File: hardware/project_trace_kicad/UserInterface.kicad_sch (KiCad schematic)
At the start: 13 parts, among them J601 Conn_01x14_Socket, J602 Conn_01x14_Pin, SW601 SW_Push, SW602 SW_Push, SW603 RotaryEncoder, SW604 RotaryEncoder, U601 SBC-OLED01.3

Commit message: Partnumbers and BOM updated
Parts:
- J601: DigikeyPN 455-1590-1-ND -> 455-1576-1-ND
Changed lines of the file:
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@@
 			)
 		)
-		(property "DigikeyPN" "455-1590-1-ND"
+		(property "DigikeyPN" "455-1576-1-ND"
 			(at 74.93 118.11 0)
 			(hide yes)

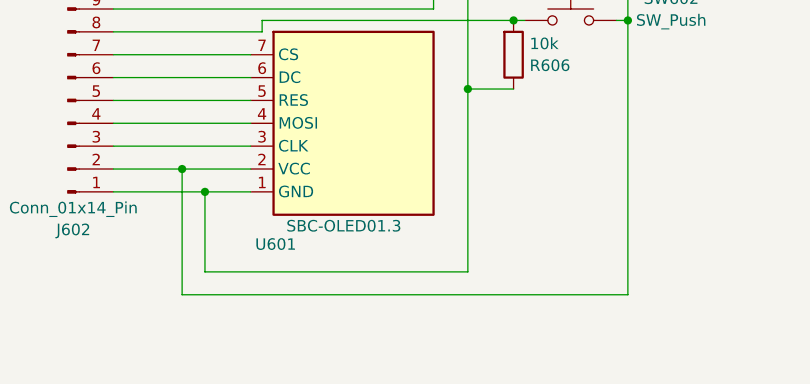
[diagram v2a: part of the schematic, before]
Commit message: Implement new DiffAmp, Small Improvements
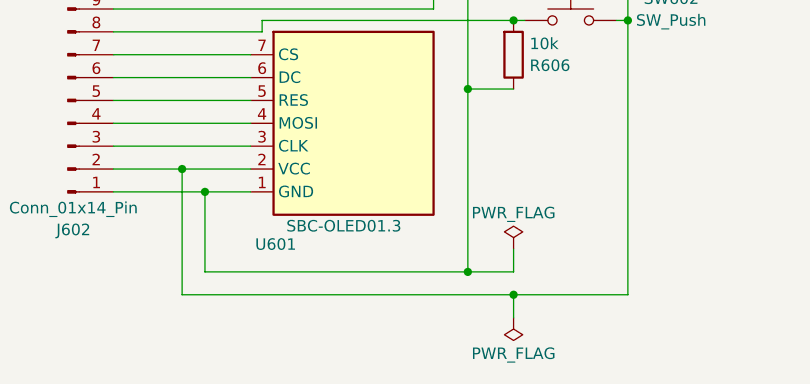
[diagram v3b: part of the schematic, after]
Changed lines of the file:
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@@
+	)
+	(junction
+		(at 147.32 144.78)
+		(diameter 0)
+		(color 0 0 0 0)
 	)
 	(junction
@@
 	)
 	(junction
+		(at 142.24 142.24)
+		(diameter 0)
+		(color 0 0 0 0)
+	)
+	(junction
 		(at 147.32 101.6)
 		(diameter 0)
@@
 	(wire
 		(pts
-			(xy 110.49 144.78) (xy 160.02 144.78)
+			(xy 110.49 144.78) (xy 147.32 144.78)
 		)
 		(stroke
@@
 	(wire
 		(pts
+			(xy 147.32 144.78) (xy 160.02 144.78)
+		)
+		(stroke
+			(width 0)
+			(type default)
+		)
+	)
+	(wire
+		(pts
 			(xy 152.4 44.45) (xy 151.13 44.45)
 		)
@@
 	(wire
 		(pts
+			(xy 147.32 144.78) (xy 147.32 147.32)
+		)
+		(stroke
+			(width 0)
+			(type default)
+		)
+	)
+	(wire
+		(pts
 			(xy 142.24 73.66) (xy 143.51 73.66)
 		)
@@
 	(wire
 		(pts
+			(xy 147.32 142.24) (xy 142.24 142.24)
+		)
+		(stroke
+			(width 0)
+			(type default)
+		)
+	)
+	(wire
+		(pts
 			(xy 154.94 82.55) (xy 157.48 82.55)
 		)
@@
 		(pts
 			(xy 151.13 73.66) (xy 152.4 73.66)
+		)
+		(stroke
+			(width 0)
+			(type default)
+		)
+	)
+	(wire
+		(pts
+			(xy 147.32 139.7) (xy 147.32 142.24)
 		)
 		(stroke
@@
 	)
 	(symbol
+		(lib_id "power:PWR_FLAG")
+		(at 147.32 139.7 0)
+		(unit 1)
+		(body_style 1)
+		(exclude_from_sim no)
+		(in_bom yes)
+		(on_board yes)
+		(in_pos_files yes)
+		(dnp no)
+		(fields_autoplaced yes)
+		(property "Reference" "#FLG0601"
+			(at 147.32 137.795 0)
+			(hide yes)
+			(show_name no)
+			(do_not_autoplace no)
+			(effects
+				(font
+					(size 1.27 1.27)
+				)
+			)
+		)
+		(property "Value" "PWR_FLAG"
+			(at 147.32 135.6952 0)
+			(show_name no)
+			(do_not_autoplace no)
+			(effects
+				(font
+					(size 1.27 1.27)
+				)
+			)
+		)
+		(property "Footprint" ""
+			(at 147.32 139.7 0)
+			(hide yes)
+			(show_name no)
+			(do_not_autoplace no)
+			(effects
+				(font
+					(size 1.27 1.27)
+				)
+			)
+		)
+		(property "Datasheet" ""
+			(at 147.32 139.7 0)
+			(hide yes)
+			(show_name no)
+			(do_not_autoplace no)
+			(effects
+				(font
+					(size 1.27 1.27)
+				)
+			)
+		)
+		(property "Description" "Special symbol for telling ERC where power comes from"
+			(at 147.32 139.7 0)
+			(hide yes)
+			(show_name no)
+			(do_not_autoplace no)
+			(effects
+				(font
+					(size 1.27 1.27)
+				)
+			)
+		)
+		(pin "1"
+		)
+		(instances
+			(project "project_trace_kicad"
+				(path "/af51f4e5-b952-4b0e-baf2-78a72fb86fcd/9647d892-1f14-4449-8bb1-1c7676664973"
+					(reference "#FLG0601")
+					(unit 1)
+				)
+			)
+		)
+	)
+	(symbol
 		(lib_id "Device:R")
 		(at 147.32 106.68 0)
@@
 					(unit 1)
 				)
+			)
+		)
+	)
+	(symbol
+		(lib_id "power:PWR_FLAG")
+		(at 147.32 147.32 0)
+		(mirror x)
+		(unit 1)
+		(body_style 1)
+		(exclude_from_sim no)
+		(in_bom yes)
+		(on_board yes)
+		(in_pos_files yes)
+		(dnp no)
+		(property "Reference" "#FLG0602"
+			(at 147.32 149.225 0)
+			(hide yes)
+			(show_name no)
+			(do_not_autoplace no)
+			(effects
+				(font
+					(size 1.27 1.27)
+				)
+			)
+		)
+		(property "Value" "PWR_FLAG"
+			(at 147.32 151.3248 0)
+			(show_name no)
+			(do_not_autoplace no)
+			(effects
+				(font
+					(size 1.27 1.27)
+				)
+			)
+		)
+		(property "Footprint" ""
+			(at 147.32 147.32 0)
+			(hide yes)
+			(show_name no)
+			(do_not_autoplace no)
+			(effects
+				(font
+					(size 1.27 1.27)
+				)
+			)
+		)
+		(property "Datasheet" ""
+			(at 147.32 147.32 0)
+			(hide yes)
+			(show_name no)
+			(do_not_autoplace no)
+			(effects
+				(font
+					(size 1.27 1.27)
+				)
+			)
+		)
+		(property "Description" "Special symbol for telling ERC where power comes from"
+			(at 147.32 147.32 0)
+			(hide yes)
+			(show_name no)
+			(do_not_autoplace no)
+			(effects
+				(font
+					(size 1.27 1.27)
+				)
+			)
+		)
+		(pin "1"
+		)
+		(instances
+			(project "project_trace_kicad"
+				(path "/af51f4e5-b952-4b0e-baf2-78a72fb86fcd/9647d892-1f14-4449-8bb1-1c7676664973"
+					(reference "#FLG0602")
+					(unit 1)
+				)

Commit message: Changes to Digital
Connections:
- net UI.GND: now reaches J602.1 (Pin_1), R605.2, R606.1, U601.1 (GND)
- net UI.GND: now also SW603.C, SW604.C; no longer R601.1, R602.1, R603.1, R604.2
- net UI.VCC: now reaches J602.2 (Pin_2), SW601.2, SW602.1, U601.2 (VCC)
- net UI.VCC: now also R601.2, R602.2, R603.1, R604.2; no longer SW603.C, SW604.C
- net at J602.12 (Pin_12), SW603.B: now also R601.1; no longer R602.2
- net at J602.13 (Pin_13), SW603.A: now also R602.1; no longer R601.2
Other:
- moved on the sheet: R601, R602, R603, R604, R605, R606, SW601, SW603, SW604

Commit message: Unfinished change of UI connectivity
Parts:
- removed J601: Conn_01x14_Socket, ProjectTraceFootprints:JST_BM14B-GHS-TBT_LF__SN__N_, symbol Connector:Conn_01x14_Socket
- removed J602: Conn_01x14_Pin, symbol Connector:Conn_01x14_Pin
- removed R605, R606: 10k, Resistor_THT:R_Axial_DIN0207_L6.3mm_D2.5mm_P10.16mm_Horizontal, symbol Device:R
- removed SW601: SW_Push, symbol Switch:SW_Push
- added SW603: SW_Push, symbol Switch:SW_Push
- added UIC601, UIC602, UIC603, UIC604, UIC605, UIC606, UIC607, UIC608, UIC609, UIC610, UIC611, UIC612, UIC613, UIC614, UIC615, UIC616, UIC617, UIC618, UIC619, UIC620, UIC621: UIconnector, TestPoint:TestPoint_Pad_D2.5mm, symbol Connector:TestPoint
- renumbered SW603 to SW601
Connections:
- net +3V3: now also R601.1, R602.2, R603.1, R604.1
- net Disp.CLK: now also U601.3 (CLK), UIC610.1
- net Disp.DC: now also U601.6 (DC), UIC604.1
- net Disp.MOSI: now also U601.4 (MOSI), UIC608.1
- net Disp.RES: now also U601.5 (RES), UIC606.1
- net Disp.~{CS}: now also U601.7 (CS), UIC602.1
- net SW1: now also UIC619.1
- net SW2: now also UIC616.1
- net SW3.A: now also R601.2, UIC614.1
- net SW3.B: now also R602.1, UIC615.1
- net SW4.A: now also R603.2, UIC617.1
- net SW4.B: now also R604.2, UIC618.1
- net UI.GND: now also SW602.1, SW603.2, UIC601.1, UIC603.1, UIC605.1, UIC607.1, UIC609.1, UIC611.1, UIC613.1, UIC620.1, UIC621.1
- net UI.VCC: now also UIC612.1; no longer R601.2, R602.2, R603.1, R604.2, SW602.1
- net at SW604.A: no longer R603.2
- net at SW601.A: no longer R602.1
- net at SW604.B: no longer R604.1
- net at SW601.B: no longer R601.1
- no-connect marks 2 -> 6
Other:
- note added: "Off-board"
- note added: "Pullup from MCU"
- note removed: "CLK"
- note removed: "CS"
- note removed: "DC"
- note removed: "GND"
- note removed: "MOSI"
- note removed: "NC"
- note removed: "RES"
- note removed: "VCC"
- moved on the sheet: SW601, SW602, SW604, U601

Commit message: Review 1 issues adressed
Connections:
- net +3V3: now also UIC612.1
- net UI.GND: no longer UIC601.1, UIC603.1, UIC605.1, UIC607.1, UIC609.1, UIC611.1, UIC613.1, UIC620.1, UIC621.1
- net UI.VCC: no longer UIC612.1
- new net GND: UIC601.1, UIC603.1, UIC605.1, UIC607.1, UIC609.1, UIC611.1, UIC613.1, UIC620.1, UIC621.1
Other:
- moved on the sheet: UIC601, UIC602, UIC603, UIC604, UIC605, UIC606, UIC607, UIC608, UIC609, UIC610, UIC611, UIC612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

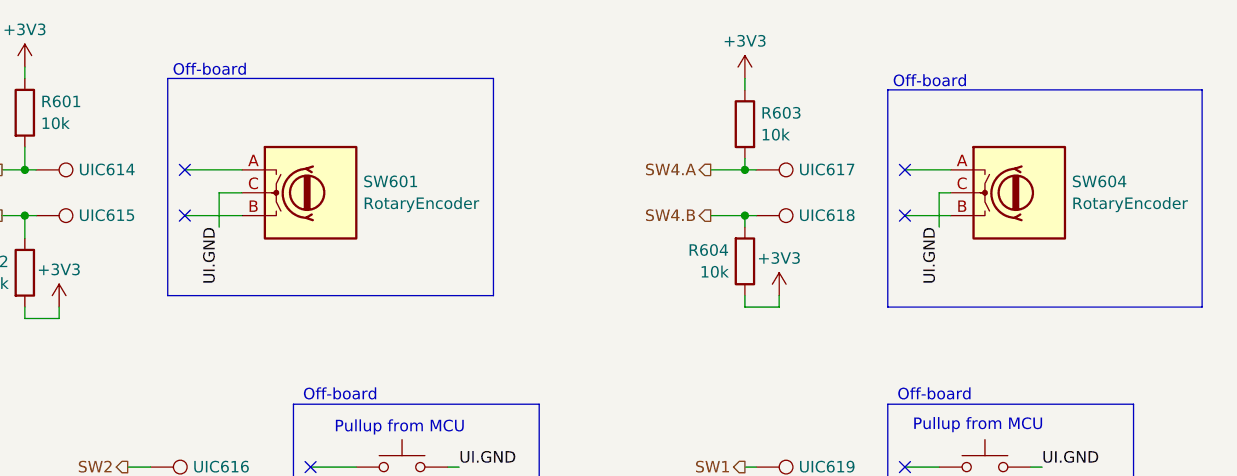
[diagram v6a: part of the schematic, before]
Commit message: Address items of internal review
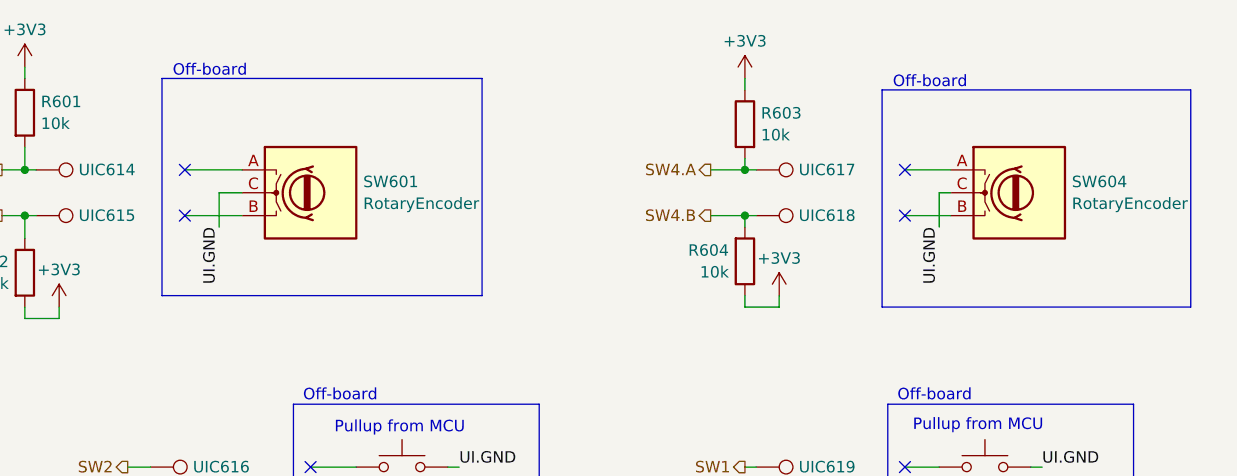
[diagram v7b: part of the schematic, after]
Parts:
- R601, R602, R603, R604: footprint Resistor_THT:R_Axial_DIN0207_L6.3mm_D2.5mm_P10.16mm_Horizontal -> Resistor_SMD:R_0603_1608Metric_Pad0.98x0.95mm_HandSolder; DigikeyPN (none) -> YAG1236CT-ND
- SW601, SW602, SW603, SW604, U601: DigikeyPN (none) -> N/A
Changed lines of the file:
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@@
 	(title_block
 		(title "Multilloscope - UserInterface")
-		(date "2026-04-06")
-		(comment 1 "Alexander N. Olsen")
+		(date "2026-04-19")
+		(rev "2")
+		(comment 1 "Reviewed by Laurits K. Hillemann")
+		(comment 2 "Alexander N. Olsen")
 	)
 	(rectangle
@@
 	)
 	(rectangle
-		(start 146.685 48.26)
-		(end 182.88 72.39)
+		(start 146.05 48.26)
+		(end 181.61 72.39)
 		(stroke
 			(width 0)
@@
 	)
 	(rectangle
-		(start 226.695 49.53)
-		(end 261.62 73.66)
+		(start 226.06 49.53)
+		(end 260.35 73.66)
 		(stroke
 			(width 0)
@@
 			)
 		)
+		(property "DigikeyPN" "N/A"
+			(at 172.72 91.44 0)
+			(hide yes)
+			(show_name no)
+			(do_not_autoplace no)
+			(effects
+				(font
+					(size 1.27 1.27)
+				)
+			)
+		)
 		(pin "2"
 		)
@@
 		(exclude_from_sim no)
 		(in_bom yes)
-		(on_board no)
+		(on_board yes)
 		(in_pos_files yes)
 		(dnp no)
@@
 			)
 		)
-		(property "Footprint" "Resistor_THT:R_Axial_DIN0207_L6.3mm_D2.5mm_P10.16mm_Horizontal"
+		(property "Footprint" "Resistor_SMD:R_0603_1608Metric_Pad0.98x0.95mm_HandSolder"
 			(at 129.032 69.85 90)
 			(hide yes)
@@
 			)
 		)
+		(property "DigikeyPN" "YAG1236CT-ND"
+			(at 130.81 69.85 0)
+			(hide yes)
+			(show_name no)
+			(do_not_autoplace no)
+			(effects
+				(font
+					(size 1.27 1.27)
+				)
+			)
+		)
 		(pin "2"
 		)
@@
 			)
 		)
+		(property "DigikeyPN" "N/A"
+			(at 162.56 60.96 0)
+			(hide yes)
+			(show_name no)
+			(do_not_autoplace no)
+			(effects
+				(font
+					(size 1.27 1.27)
+				)
+			)
+		)
 		(pin "B"
 		)
@@
 			)
 		)
+		(property "DigikeyPN" "N/A"
+			(at 241.3 60.96 0)
+			(hide yes)
+			(show_name no)
+			(do_not_autoplace no)
+			(effects
+				(font
+					(size 1.27 1.27)
+				)
+			)
+		)
 		(pin "B"
 		)
@@
 		(exclude_from_sim no)
 		(in_bom yes)
-		(on_board no)
+		(on_board yes)
 		(in_pos_files yes)
 		(dnp no)
@@
 			)
 		)
-		(property "Footprint" "Resistor_THT:R_Axial_DIN0207_L6.3mm_D2.5mm_P10.16mm_Horizontal"
+		(property "Footprint" "Resistor_SMD:R_0603_1608Metric_Pad0.98x0.95mm_HandSolder"
 			(at 209.042 68.58 90)
 			(hide yes)
@@
 			)
 		)
+		(property "DigikeyPN" "YAG1236CT-ND"
+			(at 210.82 68.58 0)
+			(hide yes)
+			(show_name no)
+			(do_not_autoplace no)
+			(effects
+				(font
+					(size 1.27 1.27)
+				)
+			)
+		)
 		(pin "2"
 		)
@@
 		(exclude_from_sim no)
 		(in_bom yes)
-		(on_board no)
+		(on_board yes)
 		(in_pos_files yes)
 		(dnp no)
@@
 			)
 		)
-		(property "Footprint" "Resistor_THT:R_Axial_DIN0207_L6.3mm_D2.5mm_P10.16mm_Horizontal"
+		(property "Footprint" "Resistor_SMD:R_0603_1608Metric_Pad0.98x0.95mm_HandSolder"
 			(at 129.032 52.07 90)
 			(hide yes)
@@
 			)
 		)
+		(property "DigikeyPN" "YAG1236CT-ND"
+			(at 130.81 52.07 0)
+			(hide yes)
+			(show_name no)
+			(do_not_autoplace no)
+			(effects
+				(font
+					(size 1.27 1.27)
+				)
+			)
+		)
 		(pin "2"
 		)
@@
 		(exclude_from_sim no)
 		(in_bom yes)
-		(on_board no)
+		(on_board yes)
 		(in_pos_files yes)
 		(dnp no)
@@
 			)
 		)
-		(property "Footprint" "Resistor_THT:R_Axial_DIN0207_L6.3mm_D2.5mm_P10.16mm_Horizontal"
+		(property "Footprint" "Resistor_SMD:R_0603_1608Metric_Pad0.98x0.95mm_HandSolder"
 			(at 212.598 53.34 90)
 			(hide yes)
@@
 			)
 		)
+		(property "DigikeyPN" "YAG1236CT-ND"
+			(at 210.82 53.34 0)
+			(hide yes)
+			(show_name no)
+			(do_not_autoplace no)
+			(effects
+				(font
+					(size 1.27 1.27)
+				)
+			)
+		)
 		(pin "2"
 		)
@@
 			)
 		)
+		(property "DigikeyPN" "N/A"
+			(at 116.84 143.51 0)
+			(hide yes)
+			(show_name no)
+			(do_not_autoplace no)
+			(effects
+				(font
+					(size 1.27 1.27)
+				)
+			)
+		)
 		(pin "4"
 		)
@@
 			(at 237.49 91.44 0)
 			(hide yes)
+			(show_name no)
+			(do_not_autoplace no)
+			(effects
+				(font
+					(size 1.27 1.27)
+				)
+			)
+		)
+		(property "DigikeyPN" "N/A"
+			(at 237.49 91.44 0)
+			(hide yes)

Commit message: Small Fixes, Fabrication File Check
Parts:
- renumbered UIC620 to UIC617, UIC621 to UIC618, UIC617 to UIC619, UIC618 to UIC620, UIC619 to UIC621
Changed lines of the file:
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@@
 		(dnp no)
 		(fields_autoplaced yes)
-		(property "Reference" "#PWR0604"
+		(property "Reference" "#PWR0607"
 			(at 214.63 76.2 0)
 			(hide yes)
@@
 			(project "project_trace_kicad"
 				(path "/af51f4e5-b952-4b0e-baf2-78a72fb86fcd/9647d892-1f14-4449-8bb1-1c7676664973"
-					(reference "#PWR0604")
+					(reference "#PWR0607")
 					(unit 1)
 				)
@@
 		(dnp no)
 		(fields_autoplaced yes)
-		(property "Reference" "#PWR0606"
+		(property "Reference" "#PWR0601"
 			(at 99.06 116.84 0)
 			(hide yes)
@@
 			(project "project_trace_kicad"
 				(path "/af51f4e5-b952-4b0e-baf2-78a72fb86fcd/9647d892-1f14-4449-8bb1-1c7676664973"
-					(reference "#PWR0606")
+					(reference "#PWR0601")
 					(unit 1)
 				)
@@
 		(dnp no)
 		(fields_autoplaced yes)
-		(property "Reference" "#PWR0602"
+		(property "Reference" "#PWR0604"
 			(at 134.62 77.47 0)
 			(hide yes)
@@
 			(project "project_trace_kicad"
 				(path "/af51f4e5-b952-4b0e-baf2-78a72fb86fcd/9647d892-1f14-4449-8bb1-1c7676664973"
-					(reference "#PWR0602")
+					(reference "#PWR0604")
 					(unit 1)
 				)
@@
 		(dnp no)
 		(fields_autoplaced yes)
-		(property "Reference" "UIC617"
+		(property "Reference" "UIC619"
 			(at 216.789 58.42 90)
 			(show_name no)
@@
 			(project "project_trace_kicad"
 				(path "/af51f4e5-b952-4b0e-baf2-78a72fb86fcd/9647d892-1f14-4449-8bb1-1c7676664973"
-					(reference "UIC617")
+					(reference "UIC619")
 					(unit 1)
 				)
@@
 		(dnp no)
 		(fields_autoplaced yes)
-		(property "Reference" "#PWR0607"
+		(property "Reference" "#PWR0602"
 			(at 102.87 134.62 0)
 			(hide yes)
@@
 			(project "project_trace_kicad"
 				(path "/af51f4e5-b952-4b0e-baf2-78a72fb86fcd/9647d892-1f14-4449-8bb1-1c7676664973"
-					(reference "#PWR0607")
+					(reference "#PWR0602")
 					(unit 1)
 				)
@@
 		(dnp no)
 		(fields_autoplaced yes)
-		(property "Reference" "#PWR0601"
+		(property "Reference" "#PWR0603"
 			(at 130.81 50.8 0)
 			(hide yes)
@@
 			(project "project_trace_kicad"
 				(path "/af51f4e5-b952-4b0e-baf2-78a72fb86fcd/9647d892-1f14-4449-8bb1-1c7676664973"
-					(reference "#PWR0601")
+					(reference "#PWR0603")
 					(unit 1)
 				)
@@
 		(dnp no)
 		(fields_autoplaced yes)
-		(property "Reference" "UIC621"
+		(property "Reference" "UIC618"
 			(at 185.039 118.11 90)
 			(show_name no)
@@
 			(project "project_trace_kicad"
 				(path "/af51f4e5-b952-4b0e-baf2-78a72fb86fcd/9647d892-1f14-4449-8bb1-1c7676664973"
-					(reference "UIC621")
+					(reference "UIC618")
 					(unit 1)
 				)
@@
 		(dnp no)
 		(fields_autoplaced yes)
-		(property "Reference" "UIC620"
+		(property "Reference" "UIC617"
 			(at 185.039 113.03 90)
 			(show_name no)
@@
 			(project "project_trace_kicad"
 				(path "/af51f4e5-b952-4b0e-baf2-78a72fb86fcd/9647d892-1f14-4449-8bb1-1c7676664973"
-					(reference "UIC620")
+					(reference "UIC617")
 					(unit 1)
 				)
@@
 		(dnp no)
 		(fields_autoplaced yes)
-		(property "Reference" "#PWR0603"
+		(property "Reference" "#PWR0606"
 			(at 210.82 52.07 0)
 			(hide yes)
@@
 			(project "project_trace_kicad"
 				(path "/af51f4e5-b952-4b0e-baf2-78a72fb86fcd/9647d892-1f14-4449-8bb1-1c7676664973"
-					(reference "#PWR0603")
+					(reference "#PWR0606")
 					(unit 1)
 				)
@@
 		(dnp no)
 		(fields_autoplaced yes)
-		(property "Reference" "UIC618"
+		(property "Reference" "UIC620"
 			(at 216.789 63.5 90)
 			(show_name no)
@@
 			(project "project_trace_kicad"
 				(path "/af51f4e5-b952-4b0e-baf2-78a72fb86fcd/9647d892-1f14-4449-8bb1-1c7676664973"
-					(reference "UIC618")
+					(reference "UIC620")
 					(unit 1)
 				)
@@
 		(dnp no)
 		(fields_autoplaced yes)
-		(property "Reference" "UIC619"
+		(property "Reference" "UIC621"
 			(at 216.789 91.44 90)
 			(show_name no)
@@
 			(project "project_trace_kicad"
 				(path "/af51f4e5-b952-4b0e-baf2-78a72fb86fcd/9647d892-1f14-4449-8bb1-1c7676664973"
-					(reference "UIC619")
-					(unit 1)
-				)
+					(reference "UIC621")
+					(unit 1)
+				)
